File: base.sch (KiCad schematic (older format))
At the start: 108 parts, among them J1 Screw_Terminal_01x02, J2 Out, Q2 MJD31C, Q3 IPD50R3K0CE, Q4 MJD31C, Q5 MMBTA42, Q6 MMBTA42, Q7 MMBTA42, Q8 MMBTA42, T1 FL2015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

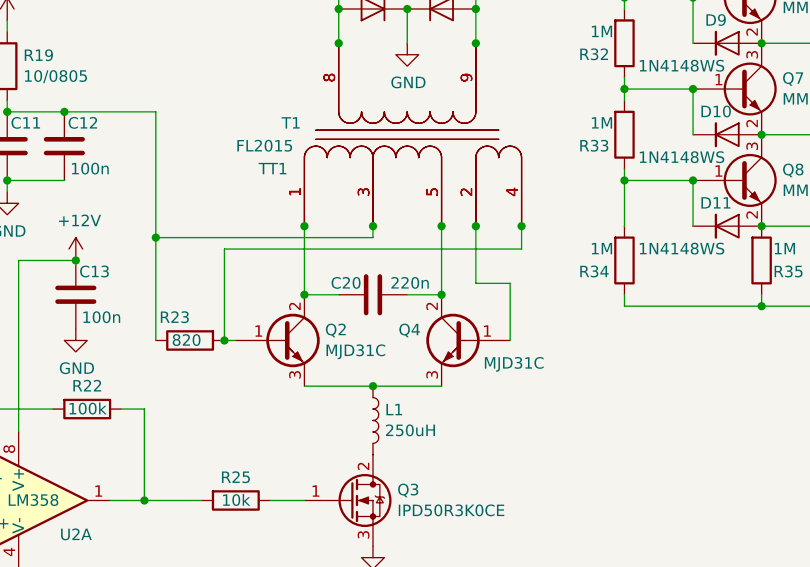
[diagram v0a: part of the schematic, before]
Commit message: Changed royer circuit cap to TH
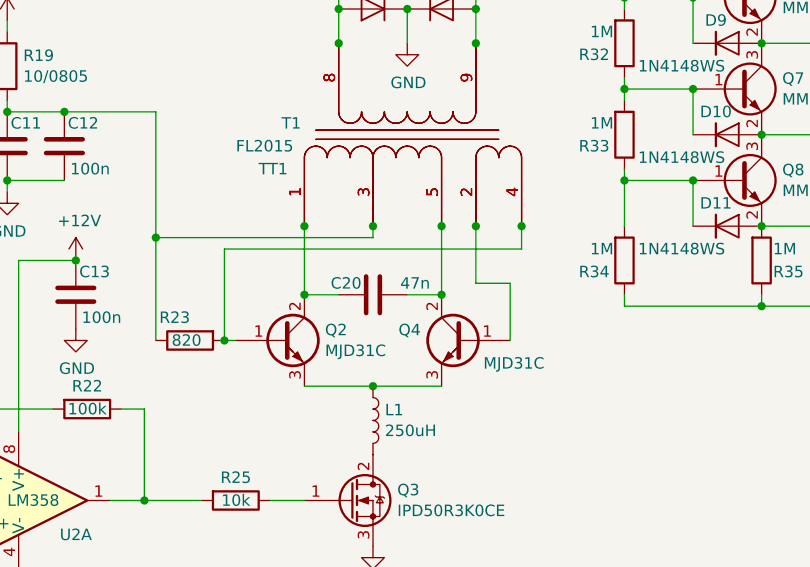
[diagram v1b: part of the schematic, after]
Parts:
- C20: value 220n -> 47n; footprint Capacitor_SMD:C_0805_2012Metric -> Capacitor_THT:C_Rect_L7.2mm_W3.5mm_P5.00mm_FKS2_FKP2_MKS2_MKP2
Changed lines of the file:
@@
 P 5400 3300
 F 0 "C20" V 5350 3350 50  0000 L CNN
-F 1 "220n" V 5350 3050 50  0000 L CNN
-F 2 "Capacitor_SMD:C_0805_2012Metric" H 5438 3150 50  0001 C CNN
+F 1 "47n" V 5350 3050 50  0000 L CNN
+F 2 "Capacitor_THT:C_Rect_L7.2mm_W3.5mm_P5.00mm_FKS2_FKP2_MKS2_MKP2" H 5438 3150 50  0001 C CNN
 F 3 "~" H 5400 3300 50  0001 C CNN
 	1    5400 3300

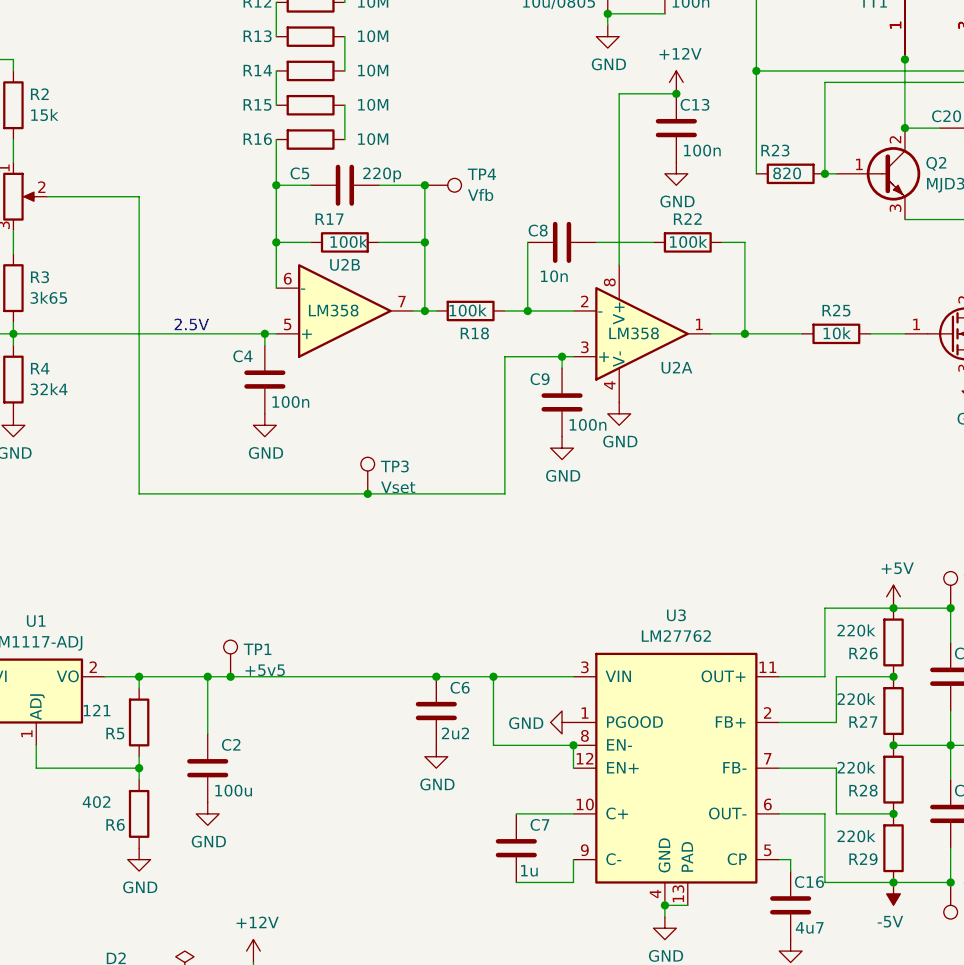
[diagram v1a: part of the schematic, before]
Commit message: Fixed some footprints and values
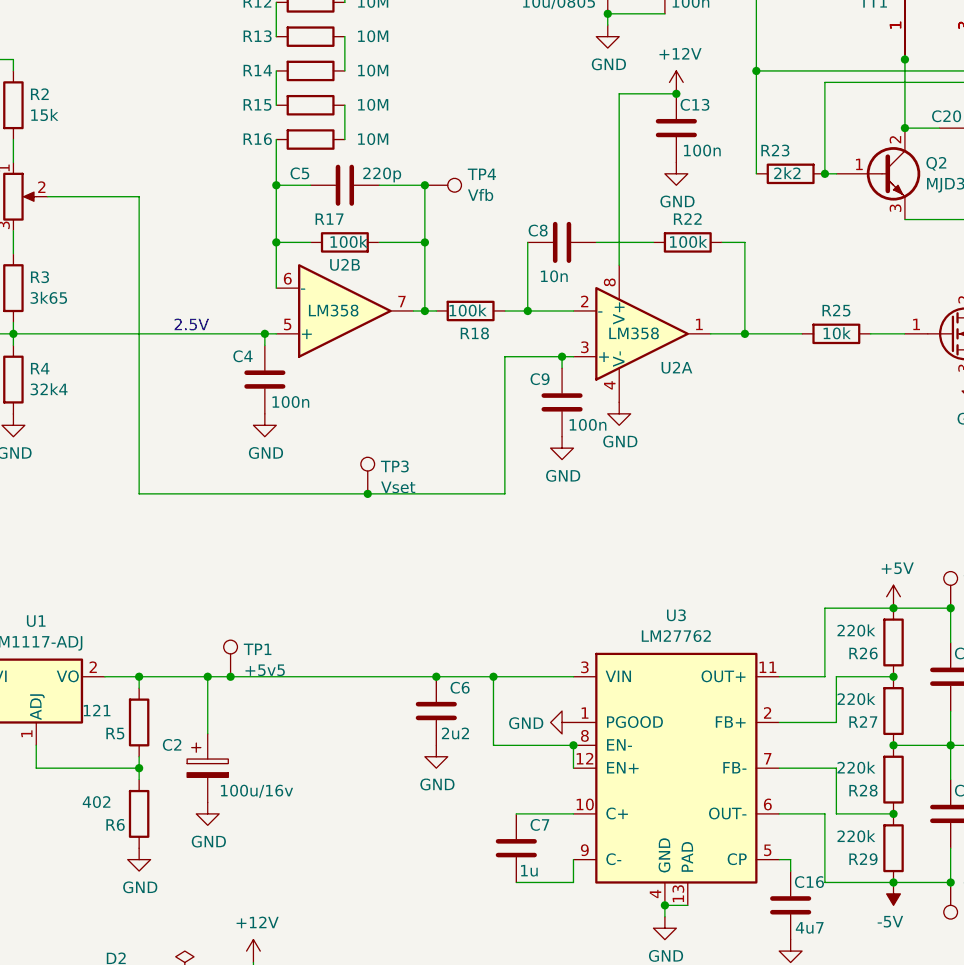
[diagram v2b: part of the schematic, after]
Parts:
- removed C2: 100u, Capacitor_SMD:C_0805_2012Metric, symbol Device:C
- added C2: 100u/16v, Capacitor_Tantalum_SMD:CP_EIA-7343-30_AVX-N, symbol Device:CP
- C1: footprint Capacitor_SMD:C_0603_1608Metric -> Capacitor_SMD:C_0805_2012Metric
- R23: value 820 -> 2k2
- R43: footprint Resistor_SMD:R_0805_2012Metric -> Resistor_SMD:R_1206_3216Metric
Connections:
- net GND: now also C2.2
- net at C6.1, R5.2, TP1.1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: now also C2.1
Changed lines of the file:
@@
 P 4600 3500
 F 0 "R23" V 4500 3500 50  0000 L CNN
-F 1 "820" V 4600 3450 50  0000 L CNN
+F 1 "2k2" V 4600 3450 50  0000 L CNN
 F 2 "Resistor_SMD:R_0805_2012Metric" V 4530 3500 50  0001 C CNN
 F 3 "~" H 4600 3500 50  0001 C CNN
@@
 $EndComp
 $Comp
-L Device:C C2
-U 1 1 5CDA3216
-P 2050 6100
-F 0 "C2" H 1900 6200 50  0000 L CNN
-F 1 "100u" H 1850 6000 50  0000 L CNN
-F 2 "Capacitor_SMD:C_0805_2012Metric" H 2088 5950 50  0001 C CNN
-F 3 "~" H 2050 6100 50  0001 C CNN
-	1    2050 6100
-	-1   0    0    -1
-$EndComp
-$Comp
 L Device:C C1
 U 1 1 5CDA3843
@@
 F 0 "C1" H 800 6200 50  0000 L CNN
 F 1 "10u" H 800 6000 50  0000 L CNN
-F 2 "Capacitor_SMD:C_0603_1608Metric" H 988 5950 50  0001 C CNN
+F 2 "Capacitor_SMD:C_0805_2012Metric" H 988 5950 50  0001 C CNN
 F 3 "~" H 950 6100 50  0001 C CNN
 	1    950  6100
@@
 F 0 "R43" H 8100 5050 50  0000 L CNN
 F 1 "1M" H 8050 4950 50  0000 L CNN
-F 2 "Resistor_SMD:R_0805_2012Metric" V 8230 5000 50  0001 C CNN
+F 2 "Resistor_SMD:R_1206_3216Metric" V 8230 5000 50  0001 C CNN
 F 3 "~" H 8300 5000 50  0001 C CNN
 	1    8300 5000
@@
 Wire Wire Line
 	8000 5150 8300 5150
+$Comp
+L Device:CP C2
+U 1 1 5CDF2934
+P 2050 6100
+F 0 "C2" H 1850 6200 50  0000 L CNN
+F 1 "100u/16v" H 2100 6000 50  0000 L CNN
+F 2 "Capacitor_Tantalum_SMD:CP_EIA-7343-30_AVX-N" H 2088 5950 50  0001 C CNN
+F 3 "~" H 2050 6100 50  0001 C CNN
+	1    2050 6100
+	1    0    0    -1
+$EndComp
 $EndSCHEMATC
